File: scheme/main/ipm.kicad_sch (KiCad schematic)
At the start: 17 parts, among them U1 URB_ZP-6WR3

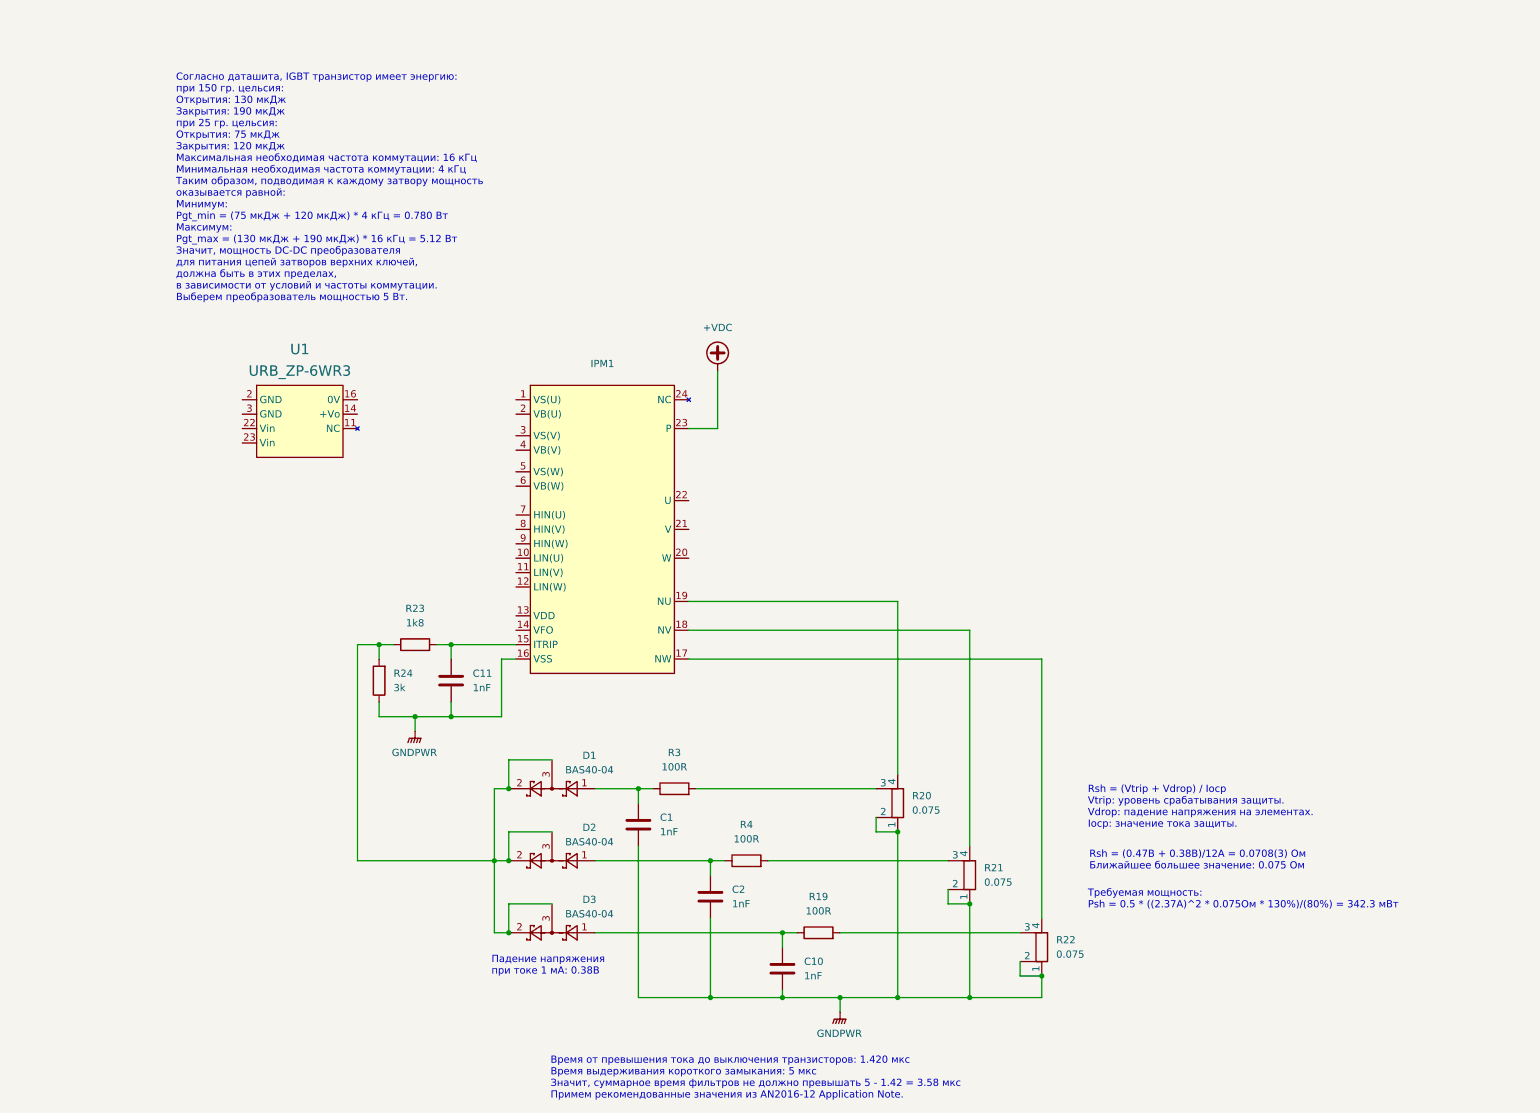
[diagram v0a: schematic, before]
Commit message: bootstrap schematic & itrip on separated list
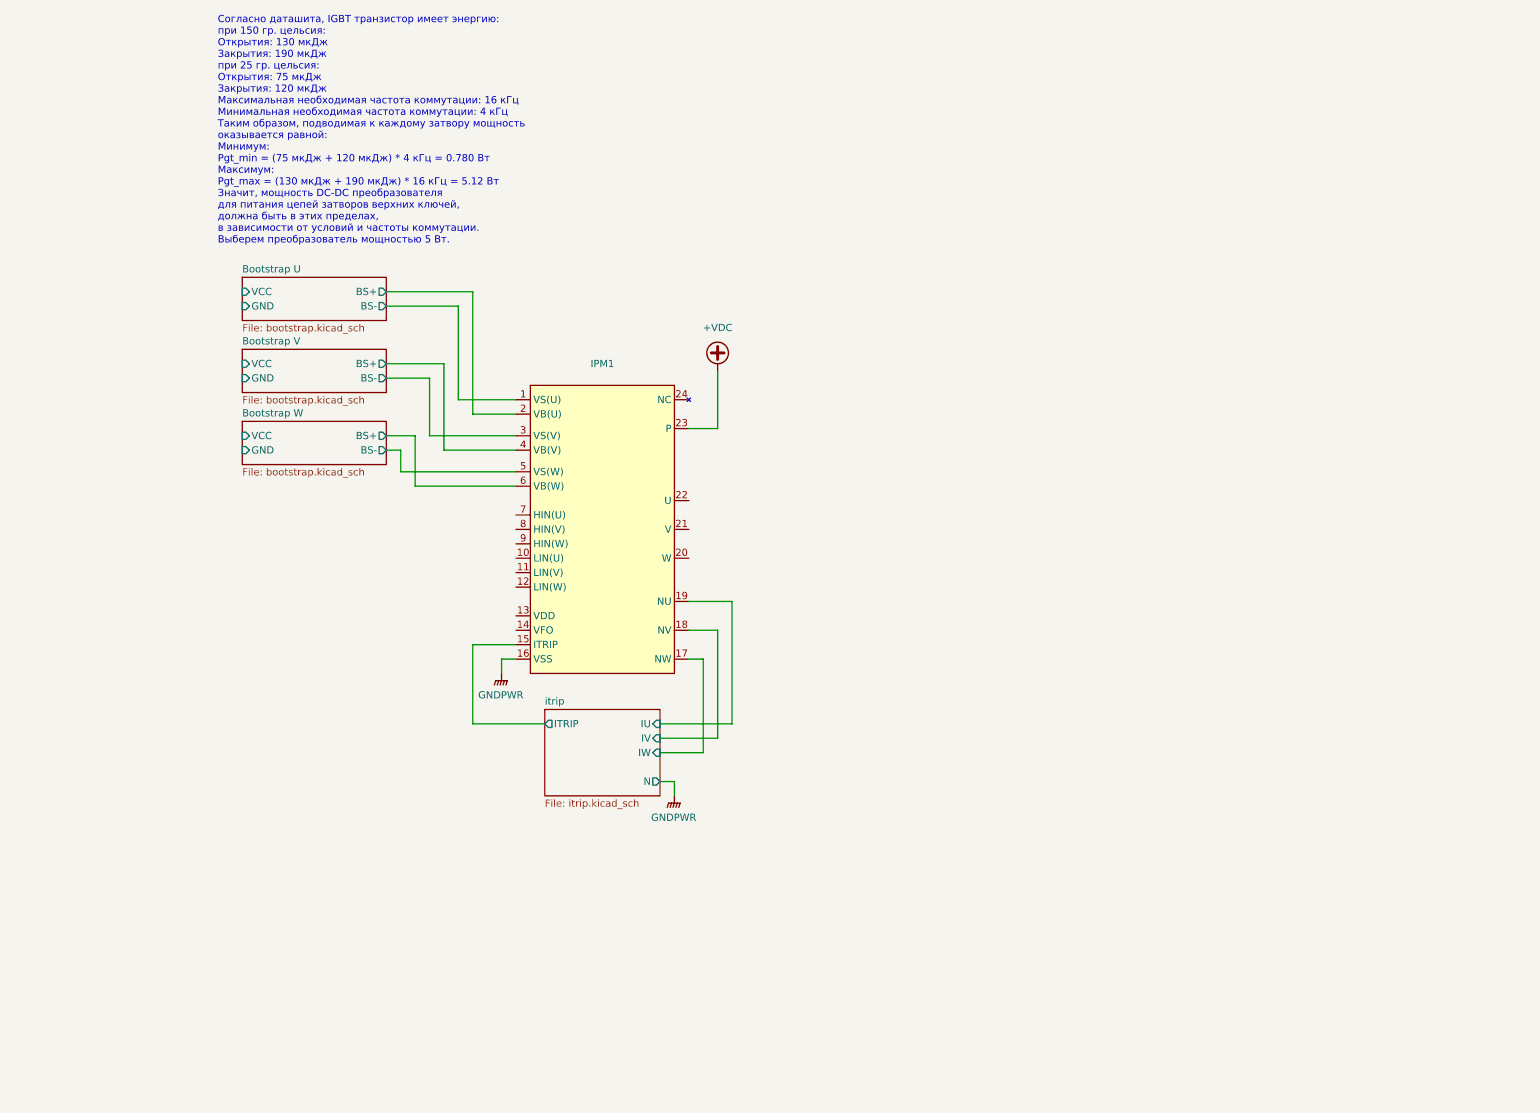
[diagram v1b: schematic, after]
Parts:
- removed C1, C10, C11, C2: 1nF, Capacitor_SMD:C_0805_2012Metric, symbol Device:C
- removed D1, D2, D3: BAS40-04, Package_TO_SOT_SMD:SOT-23, symbol Diode:BAS40-04
- removed R19, R3, R4: 100R, Resistor_SMD:R_0805_2012Metric, symbol Device:R
- removed R20, R21, R22: 0.075, Resistor_SMD:R_2512_6332Metric, symbol Device:R_Shunt
- removed R23: 1k8, Resistor_SMD:R_0805_2012Metric, symbol Device:R
- removed R24: 3k, Resistor_SMD:R_0805_2012Metric, symbol Device:R
- removed U1: URB_ZP-6WR3, main:URB_ZP-6WR3, symbol main:URB_ZP-6WR3
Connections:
- net itrip/IW: now reaches IPM1.17 (NW)
- net itrip/ITRIP: now reaches IPM1.15 (ITRIP)
- net itrip/IV: now reaches IPM1.18 (NV)
- net Bootstrap U/BS-: now reaches IPM1.1 (VS(U))
- net itrip/IU: now reaches IPM1.19 (NU)
- net Bootstrap U/BS+: now reaches IPM1.2 (VB(U))
- net Bootstrap V/BS-: now reaches IPM1.3 (VS(V))
- net Bootstrap V/BS+: now reaches IPM1.4 (VB(V))
- net Bootstrap W/BS-: now reaches IPM1.5 (VS(W))
- net Bootstrap W/BS+: now reaches IPM1.6 (VB(W))
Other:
- added sheet Bootstrap U (bootstrap.kicad_sch)
- added sheet Bootstrap V (bootstrap.kicad_sch)
- added sheet Bootstrap W (bootstrap.kicad_sch)
- added sheet itrip (itrip.kicad_sch)
- note removed: "Rsh = (0.47В + 0.38В)/12А = 0.0708(3) Ом Ближайшее большее значение: 0.075 Ом"
- note removed: "Rsh = (Vtrip + Vdrop) / Iocp Vtrip: уровень срабатывания защиты. Vdrop: падение напряжения на элементах. Iocp: значение тока защиты."
- note removed: "Время от превышения тока до выключения транзисторов: 1.420 мкс Время выдерживания короткого замыкания: 5 мкс Значит, суммарное время фильтров не должно превышать 5 - 1.42 = 3.58 мкс Примем рекомендованные значения из AN2016-12 Application Note."
- note removed: "Падение напряжения при токе 1 мА: 0.38В"
- note removed: "Требуемая мощность: Psh = 0.5 * ((2.37А)^2 * 0.075Ом * 130%)/(80%) = 342.3 мВт"

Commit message: ipm vfo output handling scheme
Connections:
- net Vfo/vfo: now reaches IPM1.14 (VFO)
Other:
- added sheet Vfo (vfo.kicad_sch)
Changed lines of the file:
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@@
+	(wire
+		(pts
+			(xy 160.02 137.16) (xy 160.02 181.61)
+		)
+		(stroke
+			(width 0)
+			(type default)
+		)
+	)
 	(wire
 		(pts
@@
 	(wire
 		(pts
+			(xy 160.02 181.61) (xy 176.53 181.61)
+		)
+		(stroke
+			(width 0)
+			(type default)
+		)
+	)
+	(wire
+		(pts
 			(xy 200.66 101.6) (xy 205.74 101.6)
 		)
@@
 		(pts
 			(xy 160.02 80.01) (xy 160.02 96.52)
+		)
+		(stroke
+			(width 0)
+			(type default)
+		)
+	)
+	(wire
+		(pts
+			(xy 170.18 137.16) (xy 160.02 137.16)
 		)
 		(stroke
@@
 				)
 			)
+		)
+	)
+	(sheet
+		(at 176.53 179.07)
+		(size 19.05 7.62)
+		(fields_autoplaced yes)
+		(stroke
+			(width 0.1524)
+			(type solid)
+		)
+		(fill
+			(color 255 255 194 1.0000)
+		)
+		(property "Sheetname" "Vfo"
+			(at 176.53 178.3584 0)
+			(effects
+				(font
+					(size 1.27 1.27)
+				)
+				(justify left bottom)
+			)
+		)
+		(property "Sheetfile" "vfo.kicad_sch"
+			(at 176.53 187.2746 0)
+			(effects
+				(font
+					(size 1.27 1.27)
+				)
+				(justify left top)
+			)
+		)
+		(pin "vfo" input
+			(at 176.53 181.61 180)
+			(effects
+				(font
+					(size 1.27 1.27)
+				)
+				(justify left)
+			)
+		)
+		(pin "Fault" output
+			(at 195.58 181.61 0)
+			(effects
+				(font
+					(size 1.27 1.27)
+				)
+				(justify right)
+			)
+		)
+		(pin "Temp" output
+			(at 195.58 184.15 0)
+			(effects
+				(font
+					(size 1.27 1.27)
+				)
+				(justify right)
+			)
+		)
+		(instances
+			(project "main"
+				(path "/c11d1dbc-4db9-4712-8d1d-5f6f7086cded/5d407613-ca47-4478-86ea-137e1786be86"
+					(page "13")
+				)
+			)

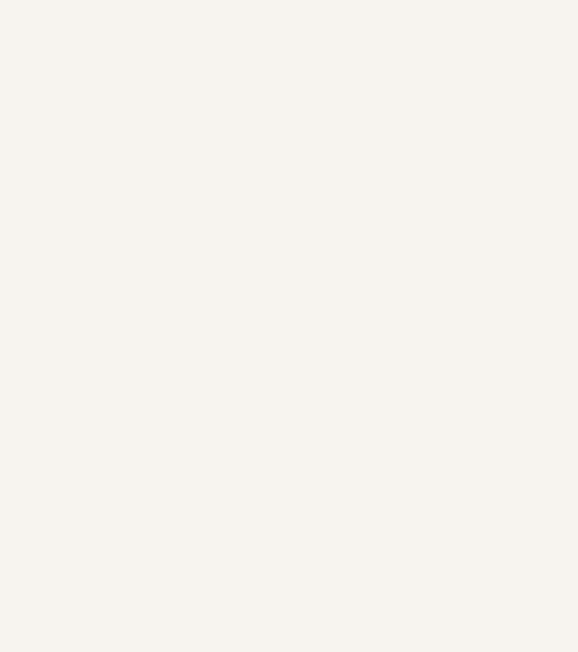
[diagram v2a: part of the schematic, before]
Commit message: vdc meas scheme
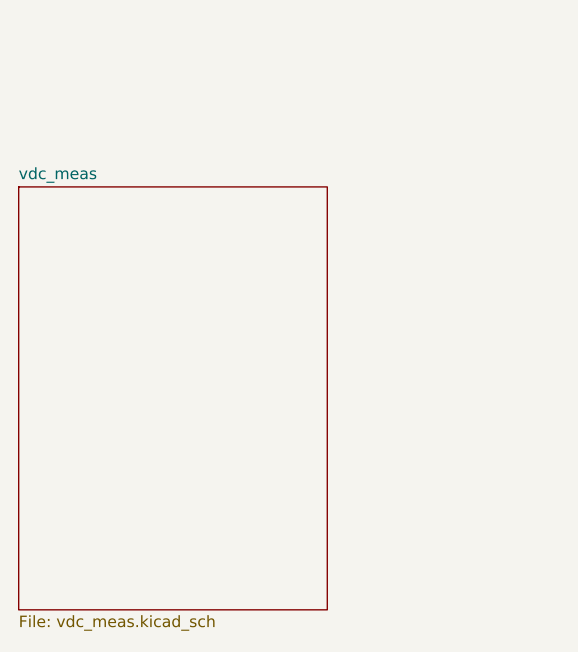
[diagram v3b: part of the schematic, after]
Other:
- added sheet vdc_meas (vdc_meas.kicad_sch)
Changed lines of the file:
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@@
+	)
+	(sheet
+		(at 81.28 153.67)
+		(size 34.29 46.99)
+		(fields_autoplaced yes)
+		(stroke
+			(width 0.1524)
+			(type solid)
+		)
+		(fill
+			(color 255 255 194 1.0000)
+		)
+		(property "Sheetname" "vdc_meas"
+			(at 81.28 152.9584 0)
+			(effects
+				(font
+					(size 1.27 1.27)
+				)
+				(justify left bottom)
+			)
+		)
+		(property "Sheetfile" "vdc_meas.kicad_sch"
+			(at 81.28 201.2446 0)
+			(effects
+				(font
+					(size 1.27 1.27)
+				)
+				(justify left top)
+			)
+		)
+		(instances
+			(project "main"
+				(path "/c11d1dbc-4db9-4712-8d1d-5f6f7086cded/5d407613-ca47-4478-86ea-137e1786be86"
+					(page "14")
+				)
+			)
+		)
 	)
 	(sheet
